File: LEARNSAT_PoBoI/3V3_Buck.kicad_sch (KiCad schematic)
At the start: 22 parts, among them U5 LT1616ES6#TRMPBF, U7 LT1616ES6#TRMPBF

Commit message: added footprints
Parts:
- C10, C6: footprint FP-CL10-IPC_B -> Vault:FP-CL10-IPC_B
- C11, C7: footprint CAPC0603(1608)100_L -> Vault:CAPC0603(1608)100_L
- C12, C5, C8, C9: footprint FP-C0603-CJ-MFG -> Vault:FP-C0603-CJ-MFG
- D11, D4: footprint FP-425-04-MFG -> Vault:FP-425-04-MFG
- D12, D3, D5, D8: footprint FP-502-01-MFG -> Vault:FP-502-01-MFG
- L1, L2: footprint INDM3532X15N -> Vault:INDM3532X15N
- R3, R5: footprint RESC1609X50X30LL10T20 -> Vault:RESC1609X50X30LL10T20
- R4, R6: footprint RESC1609X50X30NL8T20 -> Vault:RESC1609X50X30NL8T20
- U5, U7: footprint LT-S6-6-SOT-23_M -> Vault:LT-S6-6-SOT-23_M
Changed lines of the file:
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@@
 			)
 		)
-		(property "Footprint" "FP-425-04-MFG"
+		(property "Footprint" "Vault:FP-425-04-MFG"
 			(at 116.84 76.2 0)
 			(hide yes)
@@
 		(in_pos_files yes)
 		(dnp no)
-		(property "Reference" "#PWR?"
+		(property "Reference" "#PWR080"
 			(at 142.24 177.8 0)
 			(hide yes)
@@
 			(project "LEARNSAT_POBOY_v3.2.0"
 				(path "/31302da5-a970-4b2b-aa05-afcd06cb9d09/16e811dd-cb12-4b95-9c1f-bd0974340f3e"
-					(reference "#PWR?")
+					(reference "#PWR080")
 					(unit 1)
 				)
@@
 		(in_pos_files yes)
 		(dnp no)
-		(property "Reference" "#PWR?"
+		(property "Reference" "#PWR076"
 			(at 81.28 177.8 0)
 			(hide yes)
@@
 			(project "LEARNSAT_POBOY_v3.2.0"
 				(path "/31302da5-a970-4b2b-aa05-afcd06cb9d09/16e811dd-cb12-4b95-9c1f-bd0974340f3e"
-					(reference "#PWR?")
+					(reference "#PWR076")
 					(unit 1)
 				)
@@
 			)
 		)
-		(property "Footprint" "FP-C0603-CJ-MFG"
+		(property "Footprint" "Vault:FP-C0603-CJ-MFG"
 			(at 187.96 60.96 0)
 			(hide yes)
@@
 			)
 		)
-		(property "Footprint" "RESC1609X50X30LL10T20"
+		(property "Footprint" "Vault:RESC1609X50X30LL10T20"
 			(at 139.7 149.86 0)
 			(hide yes)
@@
 			)
 		)
-		(property "Footprint" "FP-CL10-IPC_B"
+		(property "Footprint" "Vault:FP-CL10-IPC_B"
 			(at 53.34 154.94 0)
 			(hide yes)
@@
 			)
 		)
-		(property "Footprint" "INDM3532X15N"
+		(property "Footprint" "Vault:INDM3532X15N"
 			(at 116.84 137.16 0)
 			(hide yes)
@@
 		(in_pos_files yes)
 		(dnp no)
-		(property "Reference" "#PWR?"
+		(property "Reference" "#PWR082"
 			(at 152.4 177.8 0)
 			(hide yes)
@@
 			(project "LEARNSAT_POBOY_v3.2.0"
 				(path "/31302da5-a970-4b2b-aa05-afcd06cb9d09/16e811dd-cb12-4b95-9c1f-bd0974340f3e"
-					(reference "#PWR?")
+					(reference "#PWR082")
 					(unit 1)
 				)
@@
 			)
 		)
-		(property "Footprint" "FP-425-04-MFG"
+		(property "Footprint" "Vault:FP-425-04-MFG"
 			(at 116.84 154.94 0)
 			(hide yes)
@@
 			)
 		)
-		(property "Footprint" "INDM3532X15N"
+		(property "Footprint" "Vault:INDM3532X15N"
 			(at 116.84 58.42 0)
 			(hide yes)
@@
 		(in_pos_files yes)
 		(dnp no)
-		(property "Reference" "#PWR?"
+		(property "Reference" "#PWR073"
 			(at 53.34 99.06 0)
 			(hide yes)
@@
 			(project "LEARNSAT_POBOY_v3.2.0"
 				(path "/31302da5-a970-4b2b-aa05-afcd06cb9d09/16e811dd-cb12-4b95-9c1f-bd0974340f3e"
-					(reference "#PWR?")
+					(reference "#PWR073")
 					(unit 1)
 				)
@@
 		(in_pos_files yes)
 		(dnp no)
-		(property "Reference" "#PWR?"
+		(property "Reference" "#PWR075"
 			(at 81.28 99.06 0)
 			(hide yes)
@@
 			(project "LEARNSAT_POBOY_v3.2.0"
 				(path "/31302da5-a970-4b2b-aa05-afcd06cb9d09/16e811dd-cb12-4b95-9c1f-bd0974340f3e"
-					(reference "#PWR?")
+					(reference "#PWR075")
 					(unit 1)
 				)
@@
 		(in_pos_files yes)
 		(dnp no)
-		(property "Reference" "#PWR?"
+		(property "Reference" "#PWR077"
 			(at 116.84 99.06 0)
 			(hide yes)
@@
 			(project "LEARNSAT_POBOY_v3.2.0"
 				(path "/31302da5-a970-4b2b-aa05-afcd06cb9d09/16e811dd-cb12-4b95-9c1f-bd0974340f3e"
-					(reference "#PWR?")
+					(reference "#PWR077")
 					(unit 1)
 				)
@@
 			)
 		)
-		(property "Footprint" "RESC1609X50X30LL10T20"
+		(property "Footprint" "Vault:RESC1609X50X30LL10T20"
 			(at 139.7 71.12 0)
 			(hide yes)
@@
 			)
 		)
-		(property "Footprint" "CAPC0603(1608)100_L"
+		(property "Footprint" "Vault:CAPC0603(1608)100_L"
 			(at 152.4 154.94 0)
 			(hide yes)
@@
 			)
 		)
-		(property "Footprint" "RESC1609X50X30NL8T20"
+		(property "Footprint" "Vault:RESC1609X50X30NL8T20"
 			(at 142.24 167.64 0)
 			(hide yes)
@@
 			)
 		)
-		(property "Footprint" "FP-502-01-MFG"
+		(property "Footprint" "Vault:FP-502-01-MFG"
 			(at 167.64 58.42 0)
 			(hide yes)
@@
 		(in_pos_files yes)
 		(dnp no)
-		(property "Reference" "#PWR?"
+		(property "Reference" "#PWR084"
 			(at 187.96 152.4 0)
 			(hide yes)
@@
 			(project "LEARNSAT_POBOY_v3.2.0"
 				(path "/31302da5-a970-4b2b-aa05-afcd06cb9d09/16e811dd-cb12-4b95-9c1f-bd0974340f3e"
-					(reference "#PWR?")
+					(reference "#PWR084")
 					(unit 1)
 				)
@@
 			)
 		)
-		(property "Footprint" "FP-CL10-IPC_B"
+		(property "Footprint" "Vault:FP-CL10-IPC_B"
 			(at 53.34 78.74 0)
 			(hide yes)
@@
 			)
 		)
-		(property "Footprint" "RESC1609X50X30NL8T20"
+		(property "Footprint" "Vault:RESC1609X50X30NL8T20"
 			(at 142.24 88.9 0)
 			(hide yes)
@@
 			)
 		)
-		(property "Footprint" "FP-C0603-CJ-MFG"
+		(property "Footprint" "Vault:FP-C0603-CJ-MFG"
 			(at 187.96 142.24 0)
 			(hide yes)
@@
 			)
 		)
-		(property "Footprint" "LT-S6-6-SOT-23_M"
+		(property "Footprint" "Vault:LT-S6-6-SOT-23_M"
 			(at 71.12 50.8 0)
 			(hide yes)
@@
 			)
 		)
-		(property "Footprint" "FP-502-01-MFG"
+		(property "Footprint" "Vault:FP-502-01-MFG"
 			(at 139.7 119.38 0)
 			(hide yes)
@@
 			)
 		)
-		(property "Footprint" "FP-502-01-MFG"
+		(property "Footprint" "Vault:FP-502-01-MFG"
 			(at 167.64 137.16 0)
 			(hide yes)
@@
 		(in_pos_files yes)
 		(dnp no)
-		(property "Reference" "#PWR?"
+		(property "Reference" "#PWR083"
 			(at 187.96 71.12 0)
 			(hide yes)
@@
 			(project "LEARNSAT_POBOY_v3.2.0"
 				(path "/31302da5-a970-4b2b-aa05-afcd06cb9d09/16e811dd-cb12-4b95-9c1f-bd0974340f3e"
-					(reference "#PWR?")
+					(reference "#PWR083")
 					(unit 1)
 				)
@@
 		(in_pos_files yes)
 		(dnp no)
-		(property "Reference" "#PWR?"
+		(property "Reference" "#PWR081"
 			(at 152.4 99.06 0)
 			(hide yes)
@@
 			(project "LEARNSAT_POBOY_v3.2.0"
 				(path "/31302da5-a970-4b2b-aa05-afcd06cb9d09/16e811dd-cb12-4b95-9c1f-bd0974340f3e"
-					(reference "#PWR?")
+					(reference "#PWR081")
 					(unit 1)
 				)
@@
 			)
 		)
-		(property "Footprint" "LT-S6-6-SOT-23_M"
+		(property "Footprint" "Vault:LT-S6-6-SOT-23_M"
 			(at 71.12 129.54 0)
 			(hide yes)
@@
 		(in_pos_files yes)
 		(dnp no)
-		(property "Reference" "#PWR?"
+		(property "Reference" "#PWR079"
 			(at 142.24 99.06 0)
 			(hide yes)
@@
 			(project "LEARNSAT_POBOY_v3.2.0"
 				(path "/31302da5-a970-4b2b-aa05-afcd06cb9d09/16e811dd-cb12-4b95-9c1f-bd0974340f3e"
-					(reference "#PWR?")
+					(reference "#PWR079")
 					(unit 1)
 				)
@@
 			)
 		)
-		(property "Footprint" "FP-C0603-CJ-MFG"
+		(property "Footprint" "Vault:FP-C0603-CJ-MFG"
 			(at 111.76 124.46 0)
 			(hide yes)
@@
 			)
 		)
-		(property "Footprint" "FP-C0603-CJ-MFG"
+		(property "Footprint" "Vault:FP-C0603-CJ-MFG"
 			(at 111.76 45.72 0)
 			(hide yes)
@@
 			)
 		)
-		(property "Footprint" "CAPC0603(1608)100_L"
+		(property "Footprint" "Vault:CAPC0603(1608)100_L"
 			(at 152.4 76.2 0)
 			(hide yes)
@@
 		(in_pos_files yes)
 		(dnp no)
-		(property "Reference" "#PWR?"
+		(property "Reference" "#PWR078"
 			(at 116.84 177.8 0)
 			(hide yes)
@@
 			(project "LEARNSAT_POBOY_v3.2.0"
 				(path "/31302da5-a970-4b2b-aa05-afcd06cb9d09/16e811dd-cb12-4b95-9c1f-bd0974340f3e"
-					(reference "#PWR?")
+					(reference "#PWR078")
 					(unit 1)
 				)
@@
 		(in_pos_files yes)
 		(dnp no)
-		(property "Reference" "#PWR?"
+		(property "Reference" "#PWR074"
 			(at 53.34 177.8 0)
 			(hide yes)
@@
 			(project "LEARNSAT_POBOY_v3.2.0"
 				(path "/31302da5-a970-4b2b-aa05-afcd06cb9d09/16e811dd-cb12-4b95-9c1f-bd0974340f3e"
-					(reference "#PWR?")
+					(reference "#PWR074")
 					(unit 1)
 				)
@@
 			)
 		)
-		(property "Footprint" "FP-502-01-MFG"
+		(property "Footprint" "Vault:FP-502-01-MFG"
 			(at 137.16 40.64 0)
 			(hide yes)

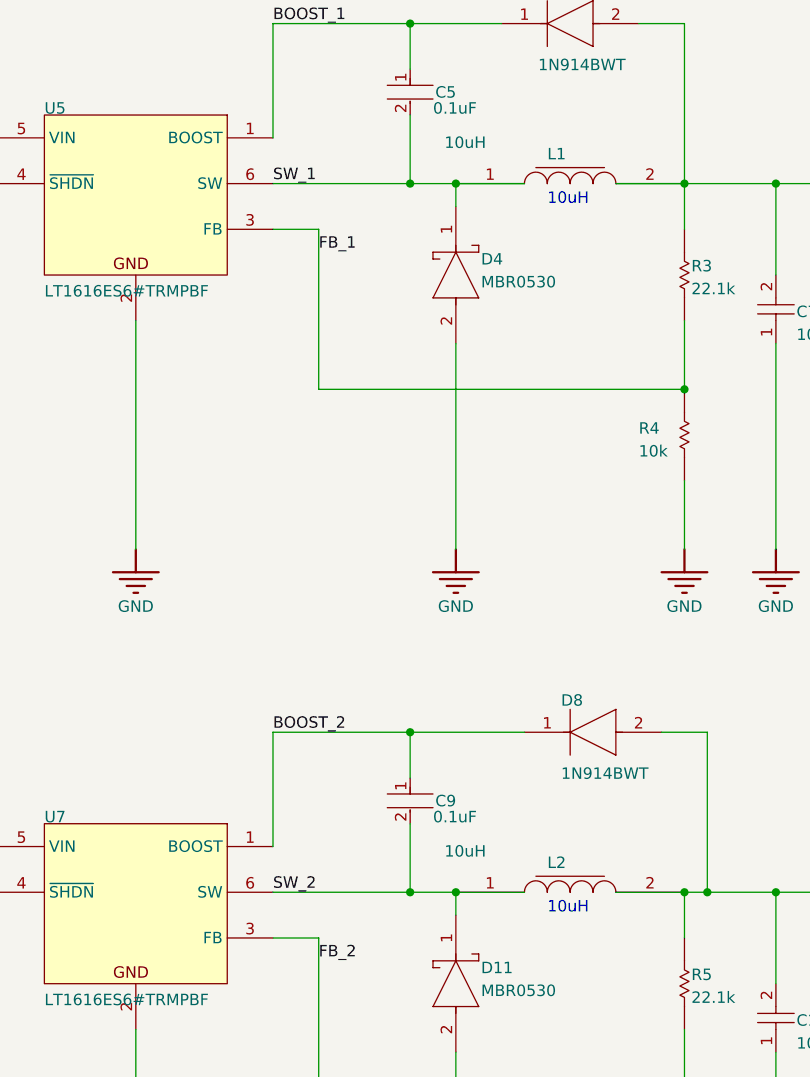
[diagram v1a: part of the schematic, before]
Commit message: moved files to right location
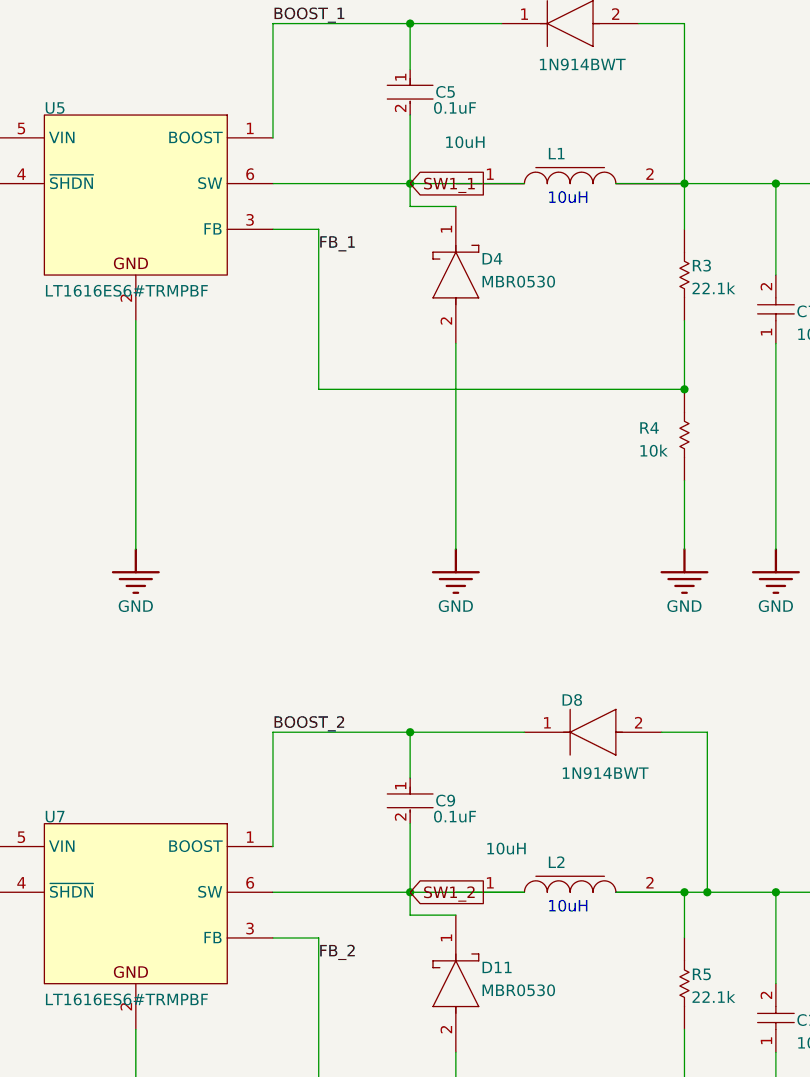
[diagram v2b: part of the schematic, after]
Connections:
- net SW1_1: now reaches C5.2, C9.2, D11.1 (C), D4.1 (C), L1.1, L2.1, U5.6 (SW), U7.6 (SW)
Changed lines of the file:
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@@
 	)
 	(junction
-		(at 116.84 137.16)
+		(at 111.76 137.16)
 		(diameter 0)
 		(color 0 0 0 0)
@@
 	)
 	(junction
-		(at 116.84 58.42)
-		(diameter 0)
-		(color 0 0 0 0)
-	)
-	(junction
 		(at 187.96 137.16)
-		(diameter 0)
-		(color 0 0 0 0)
-	)
-	(junction
-		(at 111.76 137.16)
 		(diameter 0)
 		(color 0 0 0 0)
@@
 	(wire
 		(pts
-			(xy 116.84 58.42) (xy 124.46 58.42)
+			(xy 111.76 58.42) (xy 124.46 58.42)
 		)
 		(stroke
@@
 	(wire
 		(pts
+			(xy 111.76 139.7) (xy 116.84 139.7)
+		)
+		(stroke
+			(width 0)
+			(type default)
+		)
+	)
+	(wire
+		(pts
 			(xy 101.6 142.24) (xy 101.6 160.02)
 		)
@@
 	(wire
 		(pts
-			(xy 111.76 58.42) (xy 116.84 58.42)
-		)
-		(stroke
-			(width 0)
-			(type default)
-		)
-	)
-	(wire
-		(pts
 			(xy 116.84 154.94) (xy 116.84 177.8)
 		)
@@
 	(wire
 		(pts
-			(xy 116.84 139.7) (xy 116.84 137.16)
+			(xy 111.76 139.7) (xy 111.76 137.16)
 		)
 		(stroke
@@
 	(wire
 		(pts
-			(xy 116.84 58.42) (xy 116.84 60.96)
+			(xy 111.76 58.42) (xy 111.76 60.96)
 		)
 		(stroke
@@
 	(wire
 		(pts
-			(xy 116.84 137.16) (xy 124.46 137.16)
-		)
-		(stroke
-			(width 0)
-			(type default)
-		)
-	)
-	(wire
-		(pts
 			(xy 152.4 147.32) (xy 152.4 137.16)
 		)
@@
 	(wire
 		(pts
-			(xy 111.76 137.16) (xy 116.84 137.16)
-		)
-		(stroke
-			(width 0)
-			(type default)
-		)
-	)
-	(wire
-		(pts
 			(xy 101.6 81.28) (xy 142.24 81.28)
 		)
@@
 	(wire
 		(pts
-			(xy 96.52 137.16) (xy 111.76 137.16)
+			(xy 96.52 137.16) (xy 124.46 137.16)
 		)
 		(stroke
@@
 		(pts
 			(xy 53.34 58.42) (xy 53.34 78.74)
+		)
+		(stroke
+			(width 0)
+			(type default)
+		)
+	)
+	(wire
+		(pts
+			(xy 111.76 60.96) (xy 116.84 60.96)
 		)
 		(stroke
@@
 		)
 	)
-	(label "SW_1"
-		(at 96.52 58.42 0)
-		(effects
-			(font
-				(size 1.27 1.27)
-			)
-			(justify left bottom)
-		)
-	)
 	(label ""
-		(at 116.84 137.16 0)
+		(at 113.03 137.16 0)
 		(effects
 			(font
@@
 	)
 	(label ""
-		(at 116.84 58.42 0)
+		(at 111.76 58.42 0)
 		(effects
 			(font
@@
 	(label "BOOST_1"
 		(at 96.52 40.64 0)
-		(effects
-			(font
-				(size 1.27 1.27)
-			)
-			(justify left bottom)
-		)
-	)
-	(label "SW_2"
-		(at 96.52 137.16 0)
 		(effects
 			(font
@@
 		)
 	)
+	(global_label "SW1_1"
+		(shape input)
+		(at 111.76 58.42 0)
+		(fields_autoplaced yes)
+		(effects
+			(font
+				(size 1.27 1.27)
+			)
+			(justify left)
+		)
+		(property "Intersheetrefs" "${INTERSHEET_REFS}"
+			(at 120.7927 58.42 0)
+			(hide yes)
+			(show_name no)
+			(do_not_autoplace no)
+			(effects
+				(font
+					(size 1.27 1.27)
+				)
+				(justify left)
+			)
+		)
+	)
 	(global_label "VBATT"
 		(shape input)
@@
 				)
 				(justify right)
+			)
+		)
+	)
+	(global_label "SW1_2"
+		(shape input)
+		(at 111.76 137.16 0)
+		(fields_autoplaced yes)
+		(effects
+			(font
+				(size 1.27 1.27)
+			)
+			(justify left)
+		)
+		(property "Intersheetrefs" "${INTERSHEET_REFS}"
+			(at 120.7927 137.16 0)
+			(hide yes)
+			(show_name no)
+			(do_not_autoplace no)
+			(effects
+				(font
+					(size 1.27 1.27)
+				)
+				(justify left)
 			)
 		)
@@
 		)
 		(property "INDUCTANCE" "10uH"
-			(at 115.57 133.35 0)
-			(show_name no)
-			(do_not_autoplace no)
+			(at 120.142 133.096 0)
+			(show_name no)
+			(do_not_autoplace no)
